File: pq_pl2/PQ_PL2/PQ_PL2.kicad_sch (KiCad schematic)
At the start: 70 parts, among them J1 SLW-110-01-T-S, J2 SLW-110-01-T-S, J3 SLW-110-01-T-S, J4 SLW-110-01-T-S, J5 U.FL-R-SMT, J6 MS-156C3, J7 MS-156C3, J8 U.FL-R-SMT, U1 LEE2-6+, U2 MAX2121, U3 LT5537EDDB, U4 LT3048, X1 406C35B14M

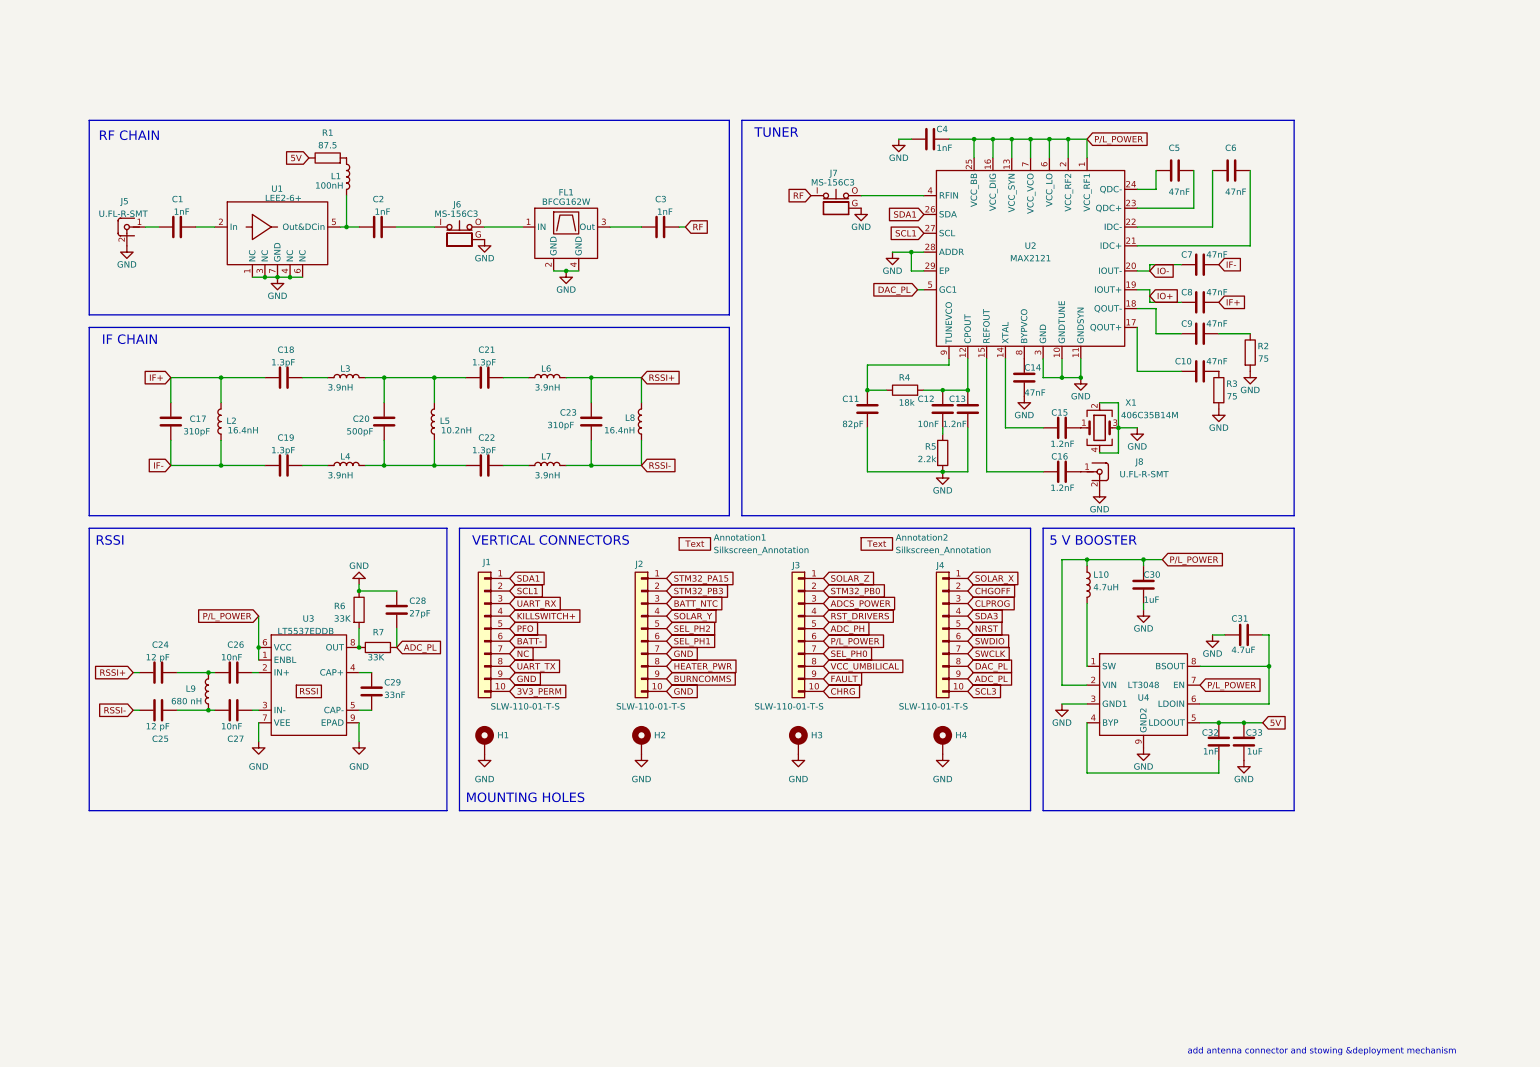
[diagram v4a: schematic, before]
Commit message: Payload 2 Schematic and PCB update. Pedning final verification and manufacturing
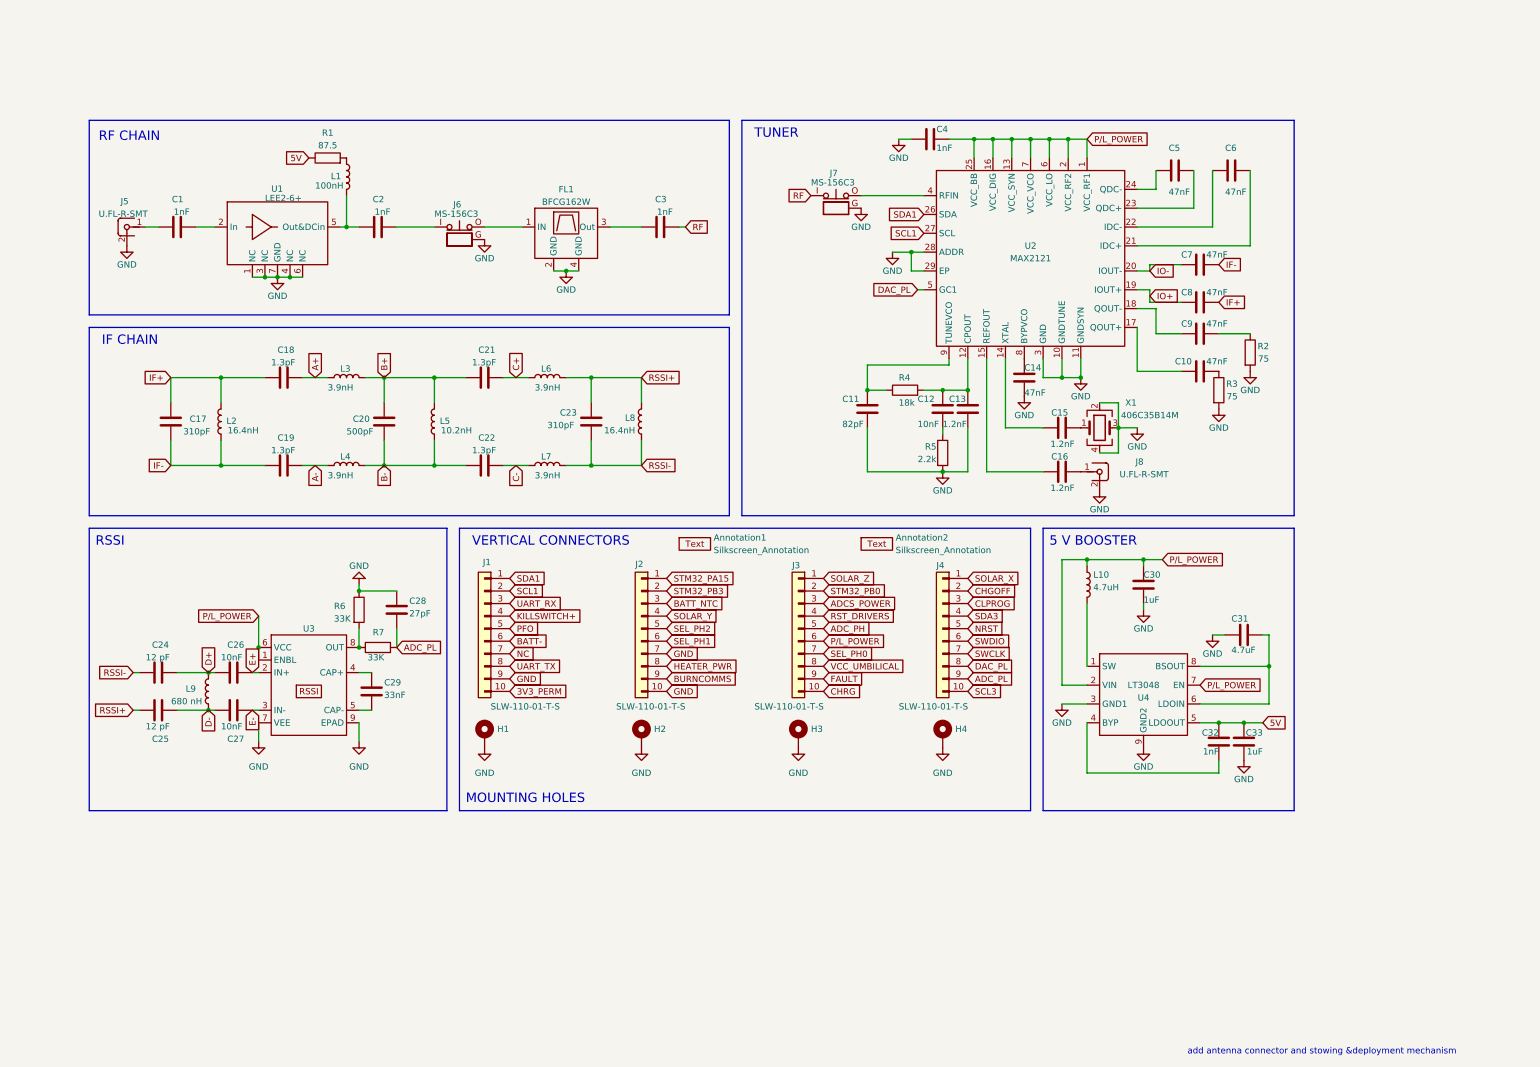
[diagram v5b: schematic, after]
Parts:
- C17, C18, C19, C20, C21, C22, C23, C24, C25, C26, C27, C7, C8: footprint Capacitor_SMD:C_0603_1608Metric -> Capacitor_SMD:C_0402_1005Metric
- J1, J2, J3, J4: footprint -nsl_connector:SLW-110-01 -> -nsl_connector:BBL-110-Y-X
- L2, L3, L4, L5, L6, L7, L8, L9: footprint Inductor_SMD:L_0603_1608Metric -> Inductor_SMD:L_0402_1005Metric
- U3: value LT5537EDDB -> ~; footprint Package_DFN_QFN:DFN-8-1EP_2x3mm_P0.5mm_EP0.56x2.15mm -> -nsl_rf:SON50P200X300X80-9N-D; CONTRIBUTOR Blothr -> (none); SPICEPRE I -> (none); SPICESYMBOLNAME LT5537EDDB#TRMPBF -> (none)
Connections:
- net RSSI+: now also C25.2; no longer C24.2
- net RSSI-: now also C24.2; no longer C25.2
- net E+: now reaches C26.1, U3.2 (IN+)
- net D+: now reaches C24.1, C26.2, L9.2
- net B+: now reaches C20.2, C21.2, L3.1, L5.1
- net A+: now reaches C18.1, L3.2
- net E-: now reaches C27.1, U3.3 (IN-)
- net D-: now reaches C25.1, C27.2, L9.1
- net C+: now reaches C21.1, L6.2
- net C-: now reaches C22.1, L7.2
- net B-: now reaches C20.1, C22.2, L4.1, L5.2
- net A-: now reaches C19.1, L4.2
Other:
- moved on the sheet: H1, H2, H3, H4

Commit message: Finished Payload 2 Schematic + PCB + BOM + Gerber + STEP Version 3.0
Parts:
- removed X1: 406C35B14M, -nsl_miscellaneous:406C35B14M, symbol -nsl_miscellaneous:406C35B14M
- added Annotation3: Silkscreen_Annotation, -nsl_symbols:NSL_long, symbol -nsl_symbols:Silkscreen_Annotation
- added Annotation4: Silkscreen_Annotation, -nsl_symbols:IEEE_logo, symbol -nsl_symbols:Silkscreen_Annotation
- added Annotation5: Silkscreen_Annotation, -nsl_symbols:UPC_positiu, symbol -nsl_symbols:Silkscreen_Annotation
- added C34: 47nF, Capacitor_SMD:C_0603_1608Metric, symbol Device:C
- added Y1: ECS-TXO-2016MV, -nsl_passive:ECSTXO201633320TR, symbol -nsl_passive:ECS-TXO-2016MV
- C11: value 82pF -> 2.2pF
- C12: value 10nF -> 270pF
- C13: value 1.2nF -> 22pF
- R4: value 18k -> 120k
- R5: value 2.2k -> 15k
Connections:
- net GND: now also C34.1, Y1.2 (GND)
- net P/L_POWER: now also C34.2, Y1.1 (Tri), Y1.4 (VDD)
- net at C15.2: now also Y1.3 (Out)
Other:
- moved on the sheet: C10, C11, C12, C13, C14, C15, C16, C4, C5, C6, C7, C8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

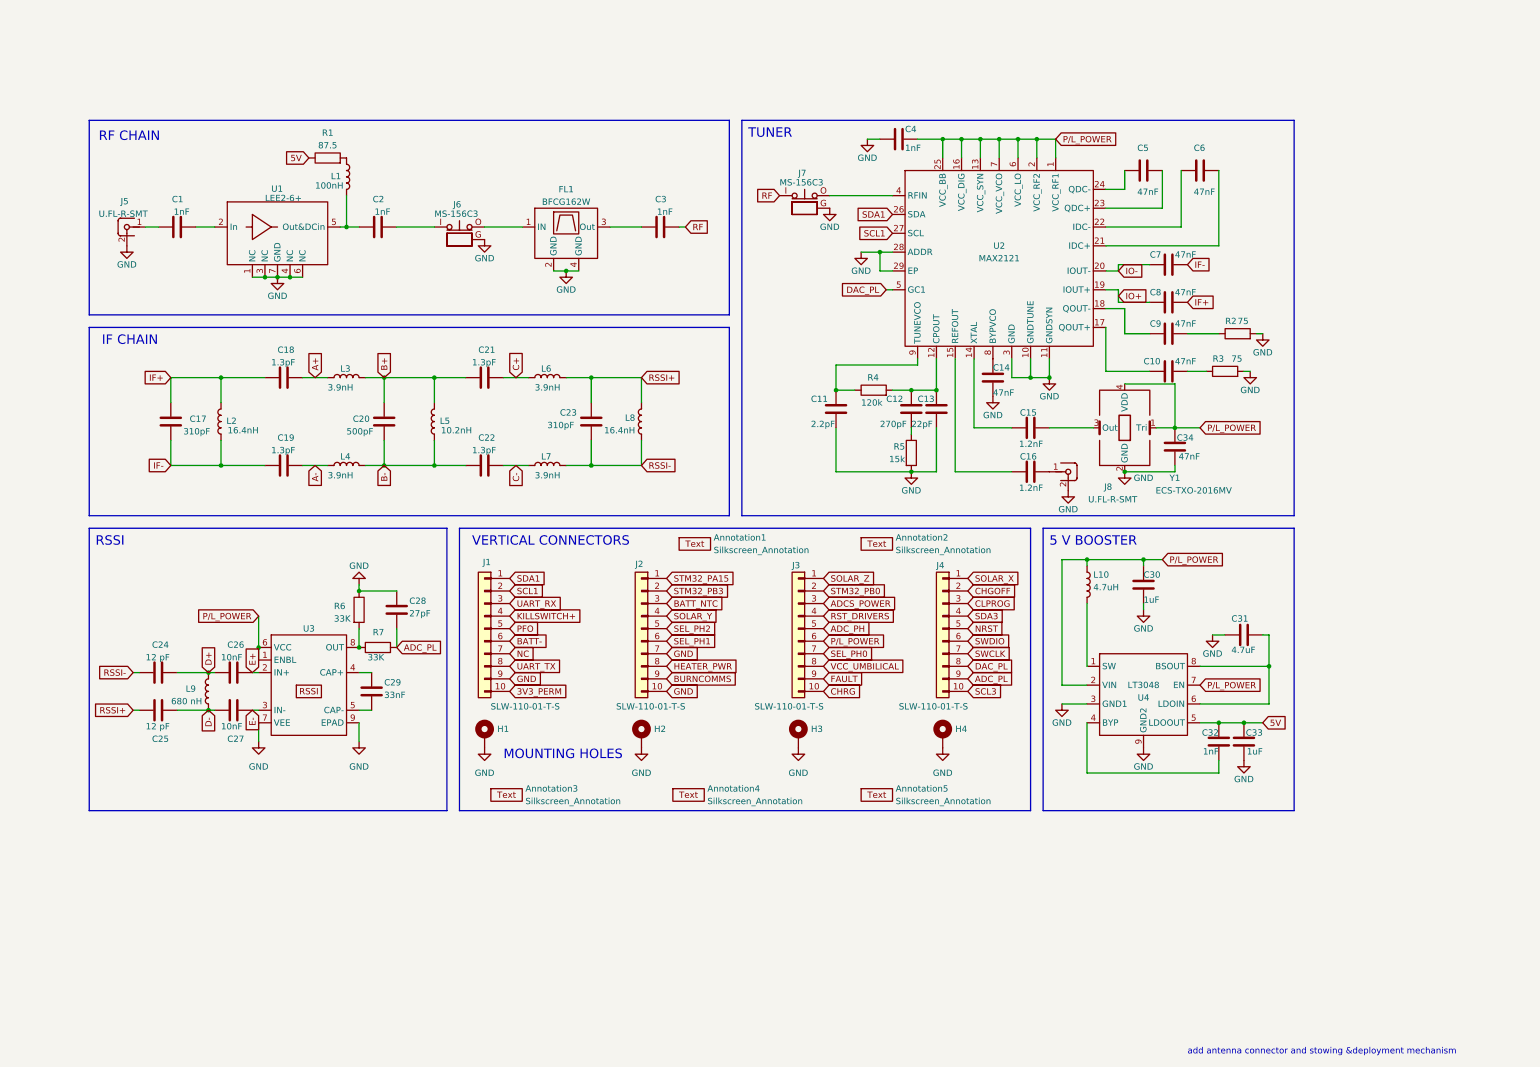
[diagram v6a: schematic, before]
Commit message: Payload 2 V3.1 - Added photodiode, associated Opamp and routing to pin STM PB0
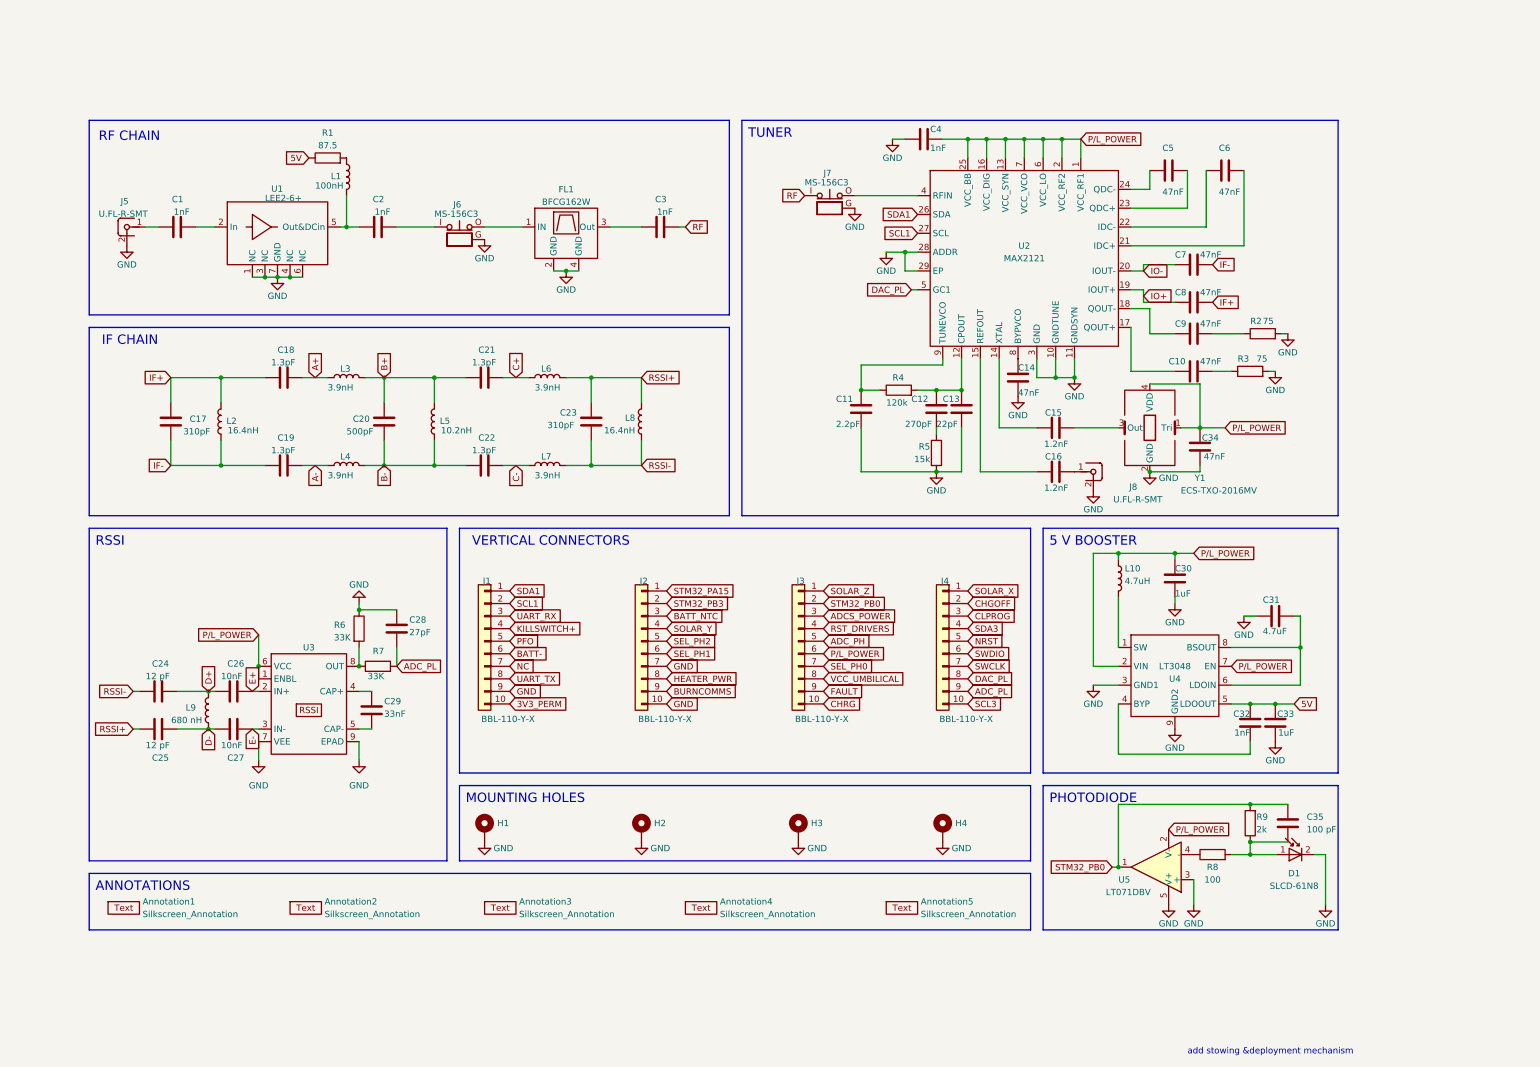
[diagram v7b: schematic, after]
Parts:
- removed J2, J3, J4: SLW-110-01-T-S, -nsl_connector:BBL-110-Y-X, symbol -nsl_connector:SLW-110-01
- added C35: 100 pF, Capacitor_SMD:C_0603_1608Metric, symbol Device:C
- added D1: SLCD-61N8, -nsl_passive:SLCD-61N8, symbol -nsl_passive:SLCD-61N8
- added J2, J3, J4: BBL-110-Y-X, -nsl_connector:BBL-110-Y-X, symbol Connector_Generic:Conn_01x10
- added R8: 100, Resistor_SMD:R_0603_1608Metric, symbol Device:R
- added R9: 2k, Resistor_SMD:R_0603_1608Metric, symbol Device:R
- added U5: LT071DBV, Package_TO_SOT_SMD:TSOT-23-5, symbol Amplifier_Operational:AD8603
- J1: value SLW-110-01-T-S -> BBL-110-Y-X; symbol -nsl_connector:SLW-110-01 -> Connector_Generic:Conn_01x10
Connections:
- net ADCS_POWER: now also J3.3 (Pin_3)
- net ADC_PH: now also J3.5 (Pin_5)
- net ADC_PL: now also J4.9 (Pin_9)
- net BATT_NTC: now also J2.3 (Pin_3)
- net BURNCOMMS: now also J2.9 (Pin_9)
- net CHGOFF: now also J4.2 (Pin_2)
- net CHRG: now also J3.10 (Pin_10)
- net CLPROG: now also J4.3 (Pin_3)
- net DAC_PL: now also J4.8 (Pin_8)
- net FAULT: now also J3.9 (Pin_9)
- net GND: now also D1.2, J2.10 (Pin_10), J2.7 (Pin_7), U5.3 (+), U5.5 (V+)
- net HEATER_PWR: now also J2.8 (Pin_8)
- net NRST: now also J4.5 (Pin_5)
- net P/L_POWER: now also J3.6 (Pin_6), U5.2 (V-)
- net RST_DRIVERS: now also J3.4 (Pin_4)
- net SCL3: now also J4.10 (Pin_10)
- net SDA3: now also J4.4 (Pin_4)
- net SEL_PH0: now also J3.7 (Pin_7)
- net SEL_PH1: now also J2.6 (Pin_6)
- net SEL_PH2: now also J2.5 (Pin_5)
- net SOLAR_X: now also J4.1 (Pin_1)
- net SOLAR_Y: now also J2.4 (Pin_4)
- net SOLAR_Z: now also J3.1 (Pin_1)
- net STM32_PA15: now also J2.1 (Pin_1)
- net STM32_PB0: now also C35.1, J3.2 (Pin_2), R9.2, U5.1
- net STM32_PB3: now also J2.2 (Pin_2)
- net SWCLK: now also J4.7 (Pin_7)
- net SWDIO: now also J4.6 (Pin_6)
- net VCC_UMBILICAL: now also J3.8 (Pin_8)
- new net: C35.2, D1.1, R8.2, R9.1
- new net: R8.1, U5.4 (-)
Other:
- note added: "ANNOTATIONS"
- note added: "PHOTODIODE"
- note added: "add stowing &deployment mechanism"
- note removed: "add antenna connector and stowing &deployment mechanism"
- moved on the sheet: Annotation1, Annotation2, Annotation3, Annotation4, Annotation5, C10, C11, C12, C13, C14, C15, C16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

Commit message: Small changes of component fields for the BOM
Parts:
- C1, C10, C11, C12, C13, C14, C15, C16, C17, C18, C19, C2, C20, C21, C22, C23, C24, C25, C26, C27, C3, C30, C31, C32, C33, C34, C4, C5, C6, C7, C8, C9: Manufacturer 1 (none) -> YAGEO; Manufacturer Part Number 1 (none) -> CC0603JRNPO0BN100; Supplier 1 (none) -> Mouser
- C28, C29: BOM_MANUFACTURER Murata Electronics -> Murata; Manufacturer 1 (none) -> Murata; Manufacturer Part Number 1 (none) -> GRM188C80J106MA73D; Supplier 1 (none) -> Mouser
- D1, FL1, H1, H2, H3, H4, J1, J2, J3, J4, U3, U4, U5, Y1: Supplier 1 (none) -> Mouser
- J5, J8: Manufacturer 1 (none) -> HRS; Manufacturer Part Number 1 (none) -> U.FL-R-SMT-1(10); Supplier 1 (none) -> Mouser
- J6, J7: Manufacturer 1 (none) -> HRS(广濑); Manufacturer Part Number 1 (none) -> MS-156C3; Supplier 1 (none) -> Mouser
- L1, L10, L2, L3, L4, L5, L6, L7, L8, L9: Manufacturer 1 (none) -> Sunlord; Manufacturer Part Number 1 (none) -> SDFL1005LR10KTF; Supplier 1 (none) -> Mouser; Supplier Part Number 1 (none) -> C576799
- R1, R2, R3, R4, R5: Supplier 1 (none) -> Mouser; Supplier Part Number 1 (none) -> C576799
- R6, R7: Manufacturer 1 (none) -> Walsin Tech Corp; Manufacturer Part Number 1 (none) -> WR06X243 JTL; Supplier 1 (none) -> Mouser; Supplier Part Number 1 (none) -> C576799
- R8: Supplier Part Number 1 603-AC0603FR-13100RL -> C469533
- R9: Supplier Part Number 1 603-RC0603FR-132KL -> C469533
- U1, U2: Supplier 1 (none) -> MiniCircuits; Supplier Part Number 1 (none) -> C576799
